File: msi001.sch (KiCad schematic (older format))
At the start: 18 parts

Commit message: msi2500 full pcb design
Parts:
- removed U?: msi001, symbol msi001
- added U2: msi001, Housings_DFN_QFN:QFN-40-1EP_6x6mm_Pitch0.5mm, symbol msi001
- C10, C11, C12, C13, C14, C15, C16, C18, C19, C20, C21, C22, C24, C25: renamed from C?; footprint (none) -> Capacitors_SMD:C_0603
- C17: renamed from C?; footprint (none) -> Capacitors_SMD:C_0805
- R2: renamed from R?; footprint (none) -> Resistors_SMD:R_0603
- gave numbers to parts that had none: 1
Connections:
- net GND: now also U2.41 (GND)
- net I_IN_N: now also U2.12 (OPIB)
- net I_IN_P: now also U2.11 (OPI)
- net LBAND-INB: now also U2.25 (INB)
- net LNAND_IN: now also U2.24 (IN)
- net Q_IN_N: now also U2.21 (OPQB)
- net Q_IN_P: now also U2.22 (OPQ)
- net REFCLK: now also U2.20 (REF-CLK)
- net SPI_CLK: now also U2.34 (CLK)
- net SPI_DATA: now also U2.35 (DATA)
- net SPI_LAT: now also U2.33 (EN)
- net UHF_400_1000MHZ: now also U2.6 (IN)
- net VDDI: now also U2.31 (VDDI)
- net VHF_120_250MHZ: now also U2.3 (IN)
- net VHF_50_120MHZ: now also U2.10 (IN)
- net VRF: now also U2.1 (VCC1), U2.2 (VCC2), U2.23 (VCC9), U2.29 (VCC10), U2.30 (VCC11), U2.32 (VDD), U2.36 (VCC12), U2.8 (VCC3)
- net at C18.2: now also U2.14 (VCC5), U2.15 (VCC6), U2.18 (VCC7), U2.19 (VCC8)
- net at C22.1, R2.2: now also U2.26 (LFILT-PC)
- net at C21.2, C22.2: now also U2.27 (CP-OUT)
- net at C21.1, C25.1, R2.1: now also U2.28 (VCO-VCC)
- net at C16.2: now also U2.39 (INB)
- net at C13.2: now also U2.4 (INB)
- net at C15.2: now also U2.40 (IN)
- net at C14.2: now also U2.7 (INB)
- net at C12.2: now also U2.9 (INB)
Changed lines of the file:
@@
 EESchema Schematic File Version 2
+LIBS:msisdr-rescue
 LIBS:power
 LIBS:device
@@
 $EndDescr
 $Comp
-L msi001 U?
-U 1 1 5C68ED43
-P 4900 3000
-F 0 "U?" H 4900 3000 39  0000 C CNN
-F 1 "msi001" H 5450 2550 39  0000 C CNN
-F 2 "" H 4900 3000 39  0001 C CNN
-F 3 "" H 4900 3000 39  0001 C CNN
-	1    4900 3000
-	1    0    0    -1
-$EndComp
-$Comp
-L GND #PWR?
+L GND #PWR15
 U 1 1 5C68EDE0
 P 3300 3100
-F 0 "#PWR?" H 3300 2850 50  0001 C CNN
+F 0 "#PWR15" H 3300 2850 50  0001 C CNN
 F 1 "GND" H 3300 2950 50  0000 C CNN
 F 2 "" H 3300 3100 50  0001 C CNN
@@
 	4350 3200 4700 3200
 $Comp
-L C C?
+L C C10
 U 1 1 5C68EE14
 P 3650 3100
-F 0 "C?" H 3675 3200 50  0000 L CNN
+F 0 "C10" H 3675 3200 50  0000 L CNN
 F 1 "10nF" H 3675 3000 50  0000 L CNN
-F 2 "" H 3688 2950 50  0001 C CNN
+F 2 "Capacitors_SMD:C_0603" H 3688 2950 50  0001 C CNN
 F 3 "" H 3650 3100 50  0001 C CNN
 	1    3650 3100
@@
 	3800 2650 4350 2650
 $Comp
-L C C?
+L C C15
 U 1 1 5C68EF3E
 P 4800 2450
-F 0 "C?" H 4825 2550 50  0000 L CNN
+F 0 "C15" H 4825 2550 50  0000 L CNN
 F 1 "100nF" H 4825 2350 50  0000 L CNN
-F 2 "" H 4838 2300 50  0001 C CNN
+F 2 "Capacitors_SMD:C_0603" H 4838 2300 50  0001 C CNN
 F 3 "" H 4800 2450 50  0001 C CNN
 	1    4800 2450
@@
 $EndComp
 $Comp
-L GND #PWR?
+L GND #PWR20
 U 1 1 5C68EF93
 P 4800 2100
-F 0 "#PWR?" H 4800 1850 50  0001 C CNN
+F 0 "#PWR20" H 4800 1850 50  0001 C CNN
 F 1 "GND" H 4800 1950 50  0000 C CNN
 F 2 "" H 4800 2100 50  0001 C CNN
@@
 HFPORT
 $Comp
-L C C?
+L C C16
 U 1 1 5C68F105
 P 5000 2250
-F 0 "C?" H 5025 2350 50  0000 L CNN
+F 0 "C16" H 5025 2350 50  0000 L CNN
 F 1 "100nF" H 5025 2150 50  0000 L CNN
-F 2 "" H 5038 2100 50  0001 C CNN
+F 2 "Capacitors_SMD:C_0603" H 5038 2100 50  0001 C CNN
 F 3 "" H 5000 2250 50  0001 C CNN
 	1    5000 2250
@@
 NoConn ~ 5350 2800
 $Comp
-L C C?
+L C C17
 U 1 1 5C68F257
 P 5350 1900
-F 0 "C?" H 5375 2000 50  0000 L CNN
+F 0 "C17" H 5375 2000 50  0000 L CNN
 F 1 "1uF" H 5375 1800 50  0000 L CNN
-F 2 "" H 5388 1750 50  0001 C CNN
+F 2 "Capacitors_SMD:C_0805" H 5388 1750 50  0001 C CNN
 F 3 "" H 5350 1900 50  0001 C CNN
 	1    5350 1900
@@
 	5350 2650 5350 2050
 $Comp
-L GND #PWR?
+L GND #PWR21
 U 1 1 5C68F2ED
 P 5350 1700
-F 0 "#PWR?" H 5350 1450 50  0001 C CNN
+F 0 "#PWR21" H 5350 1450 50  0001 C CNN
 F 1 "GND" H 5350 1550 50  0000 C CNN
 F 2 "" H 5350 1700 50  0001 C CNN
@@
 	5750 2800 5750 2350
 $Comp
-L C C?
+L C C19
 U 1 1 5C68F539
 P 5900 1900
-F 0 "C?" H 5925 2000 50  0000 L CNN
+F 0 "C19" H 5925 2000 50  0000 L CNN
 F 1 "10nF" H 5925 1800 50  0000 L CNN
-F 2 "" H 5938 1750 50  0001 C CNN
+F 2 "Capacitors_SMD:C_0603" H 5938 1750 50  0001 C CNN
 F 3 "" H 5900 1900 50  0001 C CNN
 	1    5900 1900
@@
 $EndComp
 $Comp
-L GND #PWR?
+L GND #PWR23
 U 1 1 5C68F53F
 P 5900 1700
-F 0 "#PWR?" H 5900 1450 50  0001 C CNN
+F 0 "#PWR23" H 5900 1450 50  0001 C CNN
 F 1 "GND" H 5900 1550 50  0000 C CNN
 F 2 "" H 5900 1700 50  0001 C CNN
@@
 	5850 2400 5850 2800
 $Comp
-L C C?
+L C C20
 U 1 1 5C68F624
 P 6250 1900
-F 0 "C?" H 6275 2000 50  0000 L CNN
+F 0 "C20" H 6275 2000 50  0000 L CNN
 F 1 "10nF" H 6275 1800 50  0000 L CNN
-F 2 "" H 6288 1750 50  0001 C CNN
+F 2 "Capacitors_SMD:C_0603" H 6288 1750 50  0001 C CNN
 F 3 "" H 6250 1900 50  0001 C CNN
 	1    6250 1900
@@
 $EndComp
 $Comp
-L GND #PWR?
+L GND #PWR25
 U 1 1 5C68F62A
 P 6250 1700
-F 0 "#PWR?" H 6250 1450 50  0001 C CNN
+F 0 "#PWR25" H 6250 1450 50  0001 C CNN
 F 1 "GND" H 6250 1550 50  0000 C CNN
 F 2 "" H 6250 1700 50  0001 C CNN
@@
 Connection ~ 6250 2500
 $Comp
-L C C?
+L C C23
 U 1 1 5C68F762
 P 7250 2800
-F 0 "C?" H 7275 2900 50  0000 L CNN
+F 0 "C23" H 7275 2900 50  0000 L CNN
 F 1 "10nF" H 7275 2700 50  0000 L CNN
 F 2 "" H 7288 2650 50  0001 C CNN
@@
 $EndComp
 $Comp
-L GND #PWR?
+L GND #PWR26
 U 1 1 5C68F768
 P 7450 2800
-F 0 "#PWR?" H 7450 2550 50  0001 C CNN
+F 0 "#PWR26" H 7450 2550 50  0001 C CNN
 F 1 "GND" H 7450 2650 50  0000 C CNN
 F 2 "" H 7450 2800 50  0001 C CNN
@@
 Connection ~ 6450 3100
 $Comp
-L C C?
+L C C21
 U 1 1 5C68F87D
 P 7050 3200
-F 0 "C?" H 7075 3300 50  0000 L CNN
+F 0 "C21" H 7075 3300 50  0000 L CNN
 F 1 "6800pF" V 7100 2850 50  0000 L CNN
-F 2 "" H 7088 3050 50  0001 C CNN
+F 2 "Capacitors_SMD:C_0603" H 7088 3050 50  0001 C CNN
 F 3 "" H 7050 3200 50  0001 C CNN
 	1    7050 3200
@@
 $EndComp
 $Comp
-L C C?
+L C C22
 U 1 1 5C68F90A
 P 7050 3500
-F 0 "C?" H 7075 3600 50  0000 L CNN
+F 0 "C22" H 7075 3600 50  0000 L CNN
 F 1 "6800pF" V 7100 3150 50  0000 L CNN
-F 2 "" H 7088 3350 50  0001 C CNN
+F 2 "Capacitors_SMD:C_0603" H 7088 3350 50  0001 C CNN
 F 3 "" H 7050 3500 50  0001 C CNN
 	1    7050 3500
@@
 $EndComp
 $Comp
-L C C?
+L C C25
 U 1 1 5C68F91C
 P 8050 3300
-F 0 "C?" H 8075 3400 50  0000 L CNN
+F 0 "C25" H 8075 3400 50  0000 L CNN
 F 1 "10nF" H 8075 3200 50  0000 L CNN
-F 2 "" H 8088 3150 50  0001 C CNN
+F 2 "Capacitors_SMD:C_0603" H 8088 3150 50  0001 C CNN
 F 3 "" H 8050 3300 50  0001 C CNN
 	1    8050 3300
@@
 $EndComp
 $Comp
-L R R?
+L R R2
 U 1 1 5C68F969
 P 7650 3350
-F 0 "R?" V 7730 3350 50  0000 C CNN
+F 0 "R2" V 7730 3350 50  0000 C CNN
 F 1 "390R" V 7650 3350 50  0000 C CNN
-F 2 "" V 7580 3350 50  0001 C CNN
+F 2 "Resistors_SMD:R_0603" V 7580 3350 50  0001 C CNN
 F 3 "" H 7650 3350 50  0001 C CNN
 	1    7650 3350
@@
 Connection ~ 7650 3000
 $Comp
-L GND #PWR?
+L GND #PWR28
 U 1 1 5C68FE9A
 P 8050 3550
-F 0 "#PWR?" H 8050 3300 50  0001 C CNN
+F 0 "#PWR28" H 8050 3300 50  0001 C CNN
 F 1 "GND" H 8050 3400 50  0000 C CNN
 F 2 "" H 8050 3550 50  0001 C CNN
@@
 	8050 3450 8050 3550
 $Comp
-L C C?
+L C C24
 U 1 1 5C690295
 P 7750 4000
-F 0 "C?" H 7775 4100 50  0000 L CNN
+F 0 "C24" H 7775 4100 50  0000 L CNN
 F 1 "10nF" H 7775 3900 50  0000 L CNN
-F 2 "" H 7788 3850 50  0001 C CNN
+F 2 "Capacitors_SMD:C_0603" H 7788 3850 50  0001 C CNN
 F 3 "" H 7750 4000 50  0001 C CNN
 	1    7750 4000
@@
 $EndComp
 $Comp
-L GND #PWR?
+L GND #PWR27
 U 1 1 5C69029B
 P 7950 4000
-F 0 "#PWR?" H 7950 3750 50  0001 C CNN
+F 0 "#PWR27" H 7950 3750 50  0001 C CNN
 F 1 "GND" H 7950 3850 50  0000 C CNN
 F 2 "" H 7950 4000 50  0001 C CNN
@@
 Connection ~ 6950 3800
 $Comp
-L GND #PWR?
+L GND #PWR24
 U 1 1 5C69072D
 P 6050 4800
-F 0 "#PWR?" H 6050 4550 50  0001 C CNN
+F 0 "#PWR24" H 6050 4550 50  0001 C CNN
 F 1 "GND" H 6050 4650 50  0000 C CNN
 F 2 "" H 6050 4800 50  0001 C CNN
@@
 Connection ~ 5750 4450
 $Comp
-L C C?
+L C C18
 U 1 1 5C690DC1
 P 5600 4800
-F 0 "C?" H 5625 4900 50  0000 L CNN
+F 0 "C18" H 5625 4900 50  0000 L CNN
 F 1 "10nF" H 5625 4700 50  0000 L CNN
-F 2 "" H 5638 4650 50  0001 C CNN
+F 2 "Capacitors_SMD:C_0603" H 5638 4650 50  0001 C CNN
 F 3 "" H 5600 4800 50  0001 C CNN
 	1    5600 4800
@@
 $EndComp
 $Comp
-L GND #PWR?
+L GND #PWR22
 U 1 1 5C690DC7
 P 5600 5000
-F 0 "#PWR?" H 5600 4750 50  0001 C CNN
+F 0 "#PWR22" H 5600 4750 50  0001 C CNN
 F 1 "GND" H 5600 4850 50  0000 C CNN
 F 2 "" H 5600 5000 50  0001 C CNN
@@
 NoConn ~ 5250 4350
 $Comp
-L GND #PWR?
+L GND #PWR16
 U 1 1 5C6913B6
 P 3300 3800
-F 0 "#PWR?" H 3300 3550 50  0001 C CNN
+F 0 "#PWR16" H 3300 3550 50  0001 C CNN
 F 1 "GND" H 3300 3650 50  0000 C CNN
 F 2 "" H 3300 3800 50  0001 C CNN
@@
 $EndComp
 $Comp
-L C C?
+L C C11
 U 1 1 5C6913BC
 P 3650 3800
-F 0 "C?" H 3675 3900 50  0000 L CNN
+F 0 "C11" H 3675 3900 50  0000 L CNN
 F 1 "10nF" H 3675 3700 50  0000 L CNN
-F 2 "" H 3688 3650 50  0001 C CNN
+F 2 "Capacitors_SMD:C_0603" H 3688 3650 50  0001 C CNN
 F 3 "" H 3650 3800 50  0001 C CNN
 	1    3650 3800
@@
 Connection ~ 3900 3800
 $Comp
-L GND #PWR?
+L GND #PWR17
 U 1 1 5C69151F
 P 3950 4500
-F 0 "#PWR?" H 3950 4250 50  0001 C CNN
+F 0 "#PWR17" H 3950 4250 50  0001 C CNN
 F 1 "GND" H 3950 4350 50  0000 C CNN
 F 2 "" H 3950 4500 50  0001 C CNN
@@
 $EndComp
 $Comp
-L C C?
+L C C12
 U 1 1 5C691525
 P 3950 4250
-F 0 "C?" H 3975 4350 50  0000 L CNN
+F 0 "C12" H 3975 4350 50  0000 L CNN
 F 1 "10nF" H 3975 4150 50  0000 L CNN
-F 2 "" H 3988 4100 50  0001 C CNN
+F 2 "Capacitors_SMD:C_0603" H 3988 4100 50  0001 C CNN
 F 3 "" H 3950 4250 50  0001 C CNN
 	1    3950 4250
@@
 	3950 4400 3950 4500
 $Comp
-L GND #PWR?
+L GND #PWR18
 U 1 1 5C69180E
 P 4250 4650
-F 0 "#PWR?" H 4250 4400 50  0001 C CNN
+F 0 "#PWR18" H 4250 4400 50  0001 C CNN
 F 1 "GND" H 4250 4500 50  0000 C CNN
 F 2 "" H 4250 4650 50  0001 C CNN
@@
 $EndComp
 $Comp
-L C C?
+L C C13
 U 1 1 5C691814
 P 4250 4400
-F 0 "C?" H 4275 4500 50  0000 L CNN
+F 0 "C13" H 4275 4500 50  0000 L CNN
 F 1 "10nF" H 4275 4300 50  0000 L CNN
-F 2 "" H 4288 4250 50  0001 C CNN
+F 2 "Capacitors_SMD:C_0603" H 4288 4250 50  0001 C CNN
 F 3 "" H 4250 4400 50  0001 C CNN
 	1    4250 4400
@@
 	4700 3400 4250 3400
 $Comp
-L GND #PWR?
+L GND #PWR19
 U 1 1 5C69199F
 P 4550 4850
-F 0 "#PWR?" H 4550 4600 50  0001 C CNN
+F 0 "#PWR19" H 4550 4600 50  0001 C CNN
 F 1 "GND" H 4550 4700 50  0000 C CNN
 F 2 "" H 4550 4850 50  0001 C CNN
@@
 $EndComp
 $Comp
-L C C?
+L C C14
 U 1 1 5C6919A5
 P 4550 4600
-F 0 "C?" H 4575 4700 50  0000 L CNN
+F 0 "C14" H 4575 4700 50  0000 L CNN
 F 1 "10nF" H 4575 4500 50  0000 L CNN
-F 2 "" H 4588 4450 50  0001 C CNN
+F 2 "Capacitors_SMD:C_0603" H 4588 4450 50  0001 C CNN
 F 3 "" H 4550 4600 50  0001 C CNN
 	1    4550 4600
@@
 Wire Wire Line
 	6450 3700 6350 3700
+$Comp
+L msi001 U2
+U 1 1 5C698FED
+P 4900 3000
+F 0 "U2" H 4900 3000 39  0000 C CNN
+F 1 "msi001" H 5450 2550 39  0000 C CNN
+F 2 "Housings_DFN_QFN:QFN-40-1EP_6x6mm_Pitch0.5mm" H 4900 3000 39  0001 C CNN
+F 3 "" H 4900 3000 39  0001 C CNN
+	1    4900 3000
+	1    0    0    -1
+$EndComp
 $EndSCHEMATC

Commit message: update and fix bug
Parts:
- C24: renamed from C23; footprint (none) -> Capacitors_SMD:C_0603
- renumbered C10 to C11, C11 to C12, C12 to C13, C13 to C14, C14 to C15, C15 to C16, C16 to C17, C17 to C18, C18 to C19, C19 to C20, C20 to C21, C21 to C22, C22 to C23, C24 to C25, C25 to C26
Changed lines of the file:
@@
 	4350 3200 4700 3200
 $Comp
-L C C10
+L C C11
 U 1 1 5C68EE14
 P 3650 3100
-F 0 "C10" H 3675 3200 50  0000 L CNN
+F 0 "C11" H 3675 3200 50  0000 L CNN
 F 1 "10nF" H 3675 3000 50  0000 L CNN
 F 2 "Capacitors_SMD:C_0603" H 3688 2950 50  0001 C CNN
@@
 	3800 2650 4350 2650
 $Comp
-L C C15
+L C C16
 U 1 1 5C68EF3E
 P 4800 2450
-F 0 "C15" H 4825 2550 50  0000 L CNN
+F 0 "C16" H 4825 2550 50  0000 L CNN
 F 1 "100nF" H 4825 2350 50  0000 L CNN
 F 2 "Capacitors_SMD:C_0603" H 4838 2300 50  0001 C CNN
@@
 HFPORT
 $Comp
-L C C16
+L C C17
 U 1 1 5C68F105
 P 5000 2250
-F 0 "C16" H 5025 2350 50  0000 L CNN
+F 0 "C17" H 5025 2350 50  0000 L CNN
 F 1 "100nF" H 5025 2150 50  0000 L CNN
 F 2 "Capacitors_SMD:C_0603" H 5038 2100 50  0001 C CNN
@@
 NoConn ~ 5350 2800
 $Comp
-L C C17
+L C C18
 U 1 1 5C68F257
 P 5350 1900
-F 0 "C17" H 5375 2000 50  0000 L CNN
+F 0 "C18" H 5375 2000 50  0000 L CNN
 F 1 "1uF" H 5375 1800 50  0000 L CNN
 F 2 "Capacitors_SMD:C_0805" H 5388 1750 50  0001 C CNN
@@
 Wire Wire Line
 	5350 1750 5350 1700
-Text GLabel 5550 2400 1    39   BiDi ~ 0
+Text GLabel 5550 2400 1    39   Input ~ 0
 SPI_DATA
 Wire Wire Line
@@
 	5750 2800 5750 2350
 $Comp
-L C C19
+L C C20
 U 1 1 5C68F539
 P 5900 1900
-F 0 "C19" H 5925 2000 50  0000 L CNN
+F 0 "C20" H 5925 2000 50  0000 L CNN
 F 1 "10nF" H 5925 1800 50  0000 L CNN
 F 2 "Capacitors_SMD:C_0603" H 5938 1750 50  0001 C CNN
@@
 	5850 2400 5850 2800
 $Comp
-L C C20
+L C C21
 U 1 1 5C68F624
 P 6250 1900
-F 0 "C20" H 6275 2000 50  0000 L CNN
+F 0 "C21" H 6275 2000 50  0000 L CNN
 F 1 "10nF" H 6275 1800 50  0000 L CNN
 F 2 "Capacitors_SMD:C_0603" H 6288 1750 50  0001 C CNN
@@
 Connection ~ 6250 2500
 $Comp
-L C C23
+L C C24
 U 1 1 5C68F762
 P 7250 2800
-F 0 "C23" H 7275 2900 50  0000 L CNN
+F 0 "C24" H 7275 2900 50  0000 L CNN
 F 1 "10nF" H 7275 2700 50  0000 L CNN
-F 2 "" H 7288 2650 50  0001 C CNN
+F 2 "Capacitors_SMD:C_0603" H 7288 2650 50  0001 C CNN
 F 3 "" H 7250 2800 50  0001 C CNN
 	1    7250 2800
@@
 Connection ~ 6450 3100
 $Comp
-L C C21
+L C C22
 U 1 1 5C68F87D
 P 7050 3200
-F 0 "C21" H 7075 3300 50  0000 L CNN
+F 0 "C22" H 7075 3300 50  0000 L CNN
 F 1 "6800pF" V 7100 2850 50  0000 L CNN
 F 2 "Capacitors_SMD:C_0603" H 7088 3050 50  0001 C CNN
@@
 $EndComp
 $Comp
-L C C22
+L C C23
 U 1 1 5C68F90A
 P 7050 3500
-F 0 "C22" H 7075 3600 50  0000 L CNN
+F 0 "C23" H 7075 3600 50  0000 L CNN
 F 1 "6800pF" V 7100 3150 50  0000 L CNN
 F 2 "Capacitors_SMD:C_0603" H 7088 3350 50  0001 C CNN
@@
 $EndComp
 $Comp
-L C C25
+L C C26
 U 1 1 5C68F91C
 P 8050 3300
-F 0 "C25" H 8075 3400 50  0000 L CNN
+F 0 "C26" H 8075 3400 50  0000 L CNN
 F 1 "10nF" H 8075 3200 50  0000 L CNN
 F 2 "Capacitors_SMD:C_0603" H 8088 3150 50  0001 C CNN
@@
 	8050 3450 8050 3550
 $Comp
-L C C24
+L C C25
 U 1 1 5C690295
 P 7750 4000
-F 0 "C24" H 7775 4100 50  0000 L CNN
+F 0 "C25" H 7775 4100 50  0000 L CNN
 F 1 "10nF" H 7775 3900 50  0000 L CNN
 F 2 "Capacitors_SMD:C_0603" H 7788 3850 50  0001 C CNN
@@
 Wire Wire Line
 	6050 4800 6050 4350
-Text GLabel 6600 3900 2    39   Output ~ 0
+Text GLabel 6600 3900 2    39   Input ~ 0
 Q_IN_P
 Wire Wire Line
 	6600 3900 6350 3900
-Text GLabel 6600 4050 2    39   Output ~ 0
+Text GLabel 6600 4050 2    39   Input ~ 0
 Q_IN_N
 Wire Wire Line
@@
 Connection ~ 5750 4450
 $Comp
-L C C18
+L C C19
 U 1 1 5C690DC1
 P 5600 4800
-F 0 "C18" H 5625 4900 50  0000 L CNN
+F 0 "C19" H 5625 4900 50  0000 L CNN
 F 1 "10nF" H 5625 4700 50  0000 L CNN
 F 2 "Capacitors_SMD:C_0603" H 5638 4650 50  0001 C CNN
@@
 Wire Wire Line
 	5900 4550 5900 4700
-Text GLabel 5000 4550 3    39   Output ~ 0
+Text GLabel 5000 4550 3    39   Input ~ 0
 I_IN_P
-Text GLabel 5150 4550 3    39   Output ~ 0
+Text GLabel 5150 4550 3    39   Input ~ 0
 I_IN_N
 Wire Wire Line
@@
 $EndComp
 $Comp
-L C C11
+L C C12
 U 1 1 5C6913BC
 P 3650 3800
-F 0 "C11" H 3675 3900 50  0000 L CNN
+F 0 "C12" H 3675 3900 50  0000 L CNN
 F 1 "10nF" H 3675 3700 50  0000 L CNN
 F 2 "Capacitors_SMD:C_0603" H 3688 3650 50  0001 C CNN
@@
 $EndComp
 $Comp
-L C C12
+L C C13
 U 1 1 5C691525
 P 3950 4250
-F 0 "C12" H 3975 4350 50  0000 L CNN
+F 0 "C13" H 3975 4350 50  0000 L CNN
 F 1 "10nF" H 3975 4150 50  0000 L CNN
 F 2 "Capacitors_SMD:C_0603" H 3988 4100 50  0001 C CNN
@@
 $EndComp
 $Comp
-L C C13
+L C C14
 U 1 1 5C691814
 P 4250 4400
-F 0 "C13" H 4275 4500 50  0000 L CNN
+F 0 "C14" H 4275 4500 50  0000 L CNN
 F 1 "10nF" H 4275 4300 50  0000 L CNN
 F 2 "Capacitors_SMD:C_0603" H 4288 4250 50  0001 C CNN
@@
 $EndComp
 $Comp
-L C C14
+L C C15
 U 1 1 5C6919A5
 P 4550 4600
-F 0 "C14" H 4575 4700 50  0000 L CNN
+F 0 "C15" H 4575 4700 50  0000 L CNN
 F 1 "10nF" H 4575 4500 50  0000 L CNN
 F 2 "Capacitors_SMD:C_0603" H 4588 4450 50  0001 C CNN

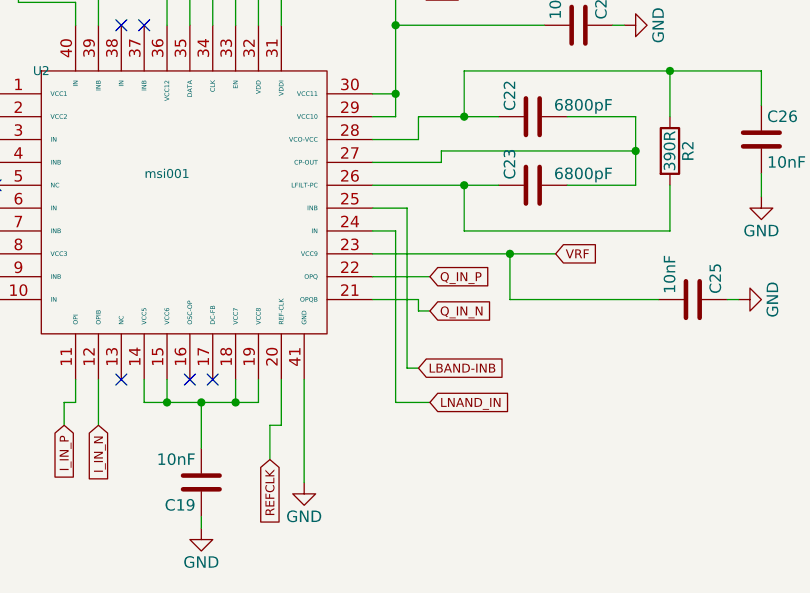
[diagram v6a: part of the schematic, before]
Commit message: fix bugs 1. not connect msi001 4 vcc to VRF 2. msi2500 VCC_GPIO connect to 1uF to GND 3. REF_CLK should use 10nF connect
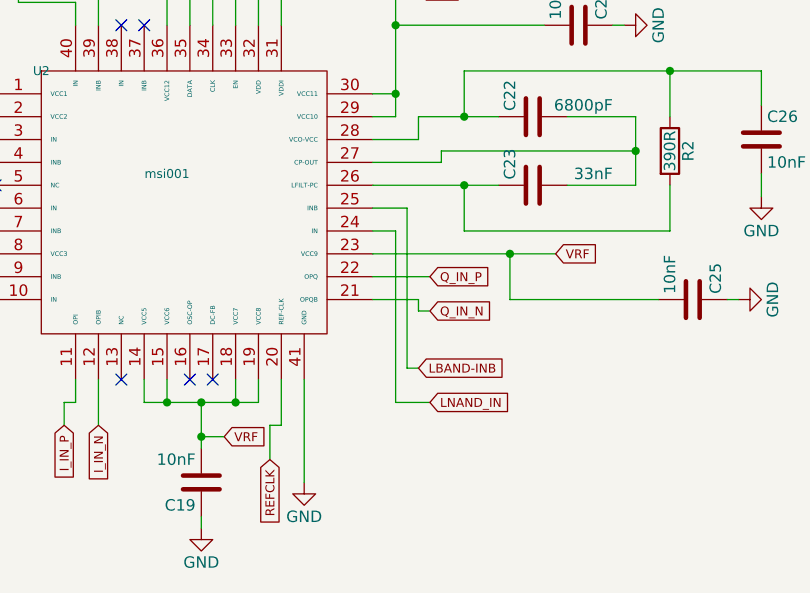
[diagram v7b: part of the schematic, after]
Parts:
- C23: value 6800pF -> 33nF
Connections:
- net VRF: now also C19.2, U2.14 (VCC5), U2.15 (VCC6), U2.18 (VCC7), U2.19 (VCC8)
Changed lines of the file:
@@
 $EndDescr
 $Comp
-L GND #PWR18
+L GND #PWR19
 U 1 1 5C68EDE0
 P 3300 3100
-F 0 "#PWR18" H 3300 2850 50  0001 C CNN
+F 0 "#PWR19" H 3300 2850 50  0001 C CNN
 F 1 "GND" H 3300 2950 50  0000 C CNN
 F 2 "" H 3300 3100 50  0001 C CNN
@@
 $EndComp
 $Comp
-L GND #PWR23
+L GND #PWR24
 U 1 1 5C68EF93
 P 4800 2100
-F 0 "#PWR23" H 4800 1850 50  0001 C CNN
+F 0 "#PWR24" H 4800 1850 50  0001 C CNN
 F 1 "GND" H 4800 1950 50  0000 C CNN
 F 2 "" H 4800 2100 50  0001 C CNN
@@
 	5350 2650 5350 2050
 $Comp
-L GND #PWR24
+L GND #PWR25
 U 1 1 5C68F2ED
 P 5350 1700
-F 0 "#PWR24" H 5350 1450 50  0001 C CNN
+F 0 "#PWR25" H 5350 1450 50  0001 C CNN
 F 1 "GND" H 5350 1550 50  0000 C CNN
 F 2 "" H 5350 1700 50  0001 C CNN
@@
 $EndComp
 $Comp
-L GND #PWR26
+L GND #PWR27
 U 1 1 5C68F53F
 P 5900 1700
-F 0 "#PWR26" H 5900 1450 50  0001 C CNN
+F 0 "#PWR27" H 5900 1450 50  0001 C CNN
 F 1 "GND" H 5900 1550 50  0000 C CNN
 F 2 "" H 5900 1700 50  0001 C CNN
@@
 $EndComp
 $Comp
-L GND #PWR28
+L GND #PWR29
 U 1 1 5C68F62A
 P 6250 1700
-F 0 "#PWR28" H 6250 1450 50  0001 C CNN
+F 0 "#PWR29" H 6250 1450 50  0001 C CNN
 F 1 "GND" H 6250 1550 50  0000 C CNN
 F 2 "" H 6250 1700 50  0001 C CNN
@@
 $EndComp
 $Comp
-L GND #PWR29
+L GND #PWR30
 U 1 1 5C68F768
 P 7450 2800
-F 0 "#PWR29" H 7450 2550 50  0001 C CNN
+F 0 "#PWR30" H 7450 2550 50  0001 C CNN
 F 1 "GND" H 7450 2650 50  0000 C CNN
 F 2 "" H 7450 2800 50  0001 C CNN
@@
 P 7050 3500
 F 0 "C23" H 7075 3600 50  0000 L CNN
-F 1 "6800pF" V 7100 3150 50  0000 L CNN
+F 1 "33nF" V 7100 3150 50  0000 L CNN
 F 2 "Capacitors_SMD:C_0603" H 7088 3350 50  0001 C CNN
 F 3 "" H 7050 3500 50  0001 C CNN
@@
 Connection ~ 7650 3000
 $Comp
-L GND #PWR31
+L GND #PWR32
 U 1 1 5C68FE9A
 P 8050 3550
-F 0 "#PWR31" H 8050 3300 50  0001 C CNN
+F 0 "#PWR32" H 8050 3300 50  0001 C CNN
 F 1 "GND" H 8050 3400 50  0000 C CNN
 F 2 "" H 8050 3550 50  0001 C CNN
@@
 $EndComp
 $Comp
-L GND #PWR30
+L GND #PWR31
 U 1 1 5C69029B
 P 7950 4000
-F 0 "#PWR30" H 7950 3750 50  0001 C CNN
+F 0 "#PWR31" H 7950 3750 50  0001 C CNN
 F 1 "GND" H 7950 3850 50  0000 C CNN
 F 2 "" H 7950 4000 50  0001 C CNN
@@
 Connection ~ 6950 3800
 $Comp
-L GND #PWR27
+L GND #PWR28
 U 1 1 5C69072D
 P 6050 4800
-F 0 "#PWR27" H 6050 4550 50  0001 C CNN
+F 0 "#PWR28" H 6050 4550 50  0001 C CNN
 F 1 "GND" H 6050 4650 50  0000 C CNN
 F 2 "" H 6050 4800 50  0001 C CNN
@@
 $EndComp
 $Comp
-L GND #PWR25
+L GND #PWR26
 U 1 1 5C690DC7
 P 5600 5000
-F 0 "#PWR25" H 5600 4750 50  0001 C CNN
+F 0 "#PWR26" H 5600 4750 50  0001 C CNN
 F 1 "GND" H 5600 4850 50  0000 C CNN
 F 2 "" H 5600 5000 50  0001 C CNN
@@
 NoConn ~ 5250 4350
 $Comp
-L GND #PWR19
+L GND #PWR20
 U 1 1 5C6913B6
 P 3300 3800
-F 0 "#PWR19" H 3300 3550 50  0001 C CNN
+F 0 "#PWR20" H 3300 3550 50  0001 C CNN
 F 1 "GND" H 3300 3650 50  0000 C CNN
 F 2 "" H 3300 3800 50  0001 C CNN
@@
 Connection ~ 3900 3800
 $Comp
-L GND #PWR20
+L GND #PWR21
 U 1 1 5C69151F
 P 3950 4500
-F 0 "#PWR20" H 3950 4250 50  0001 C CNN
+F 0 "#PWR21" H 3950 4250 50  0001 C CNN
 F 1 "GND" H 3950 4350 50  0000 C CNN
 F 2 "" H 3950 4500 50  0001 C CNN
@@
 	3950 4400 3950 4500
 $Comp
-L GND #PWR21
+L GND #PWR22
 U 1 1 5C69180E
 P 4250 4650
-F 0 "#PWR21" H 4250 4400 50  0001 C CNN
+F 0 "#PWR22" H 4250 4400 50  0001 C CNN
 F 1 "GND" H 4250 4500 50  0000 C CNN
 F 2 "" H 4250 4650 50  0001 C CNN
@@
 	4700 3400 4250 3400
 $Comp
-L GND #PWR22
+L GND #PWR23
 U 1 1 5C69199F
 P 4550 4850
-F 0 "#PWR22" H 4550 4600 50  0001 C CNN
+F 0 "#PWR23" H 4550 4600 50  0001 C CNN
 F 1 "GND" H 4550 4700 50  0000 C CNN
 F 2 "" H 4550 4850 50  0001 C CNN
@@
 	1    0    0    -1
 $EndComp
+Text GLabel 5700 4600 2    39   Input ~ 0
+VRF
+Wire Wire Line
+	5700 4600 5600 4600
+Connection ~ 5600 4600
 $EndSCHEMATC
